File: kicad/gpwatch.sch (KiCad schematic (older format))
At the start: 4 parts

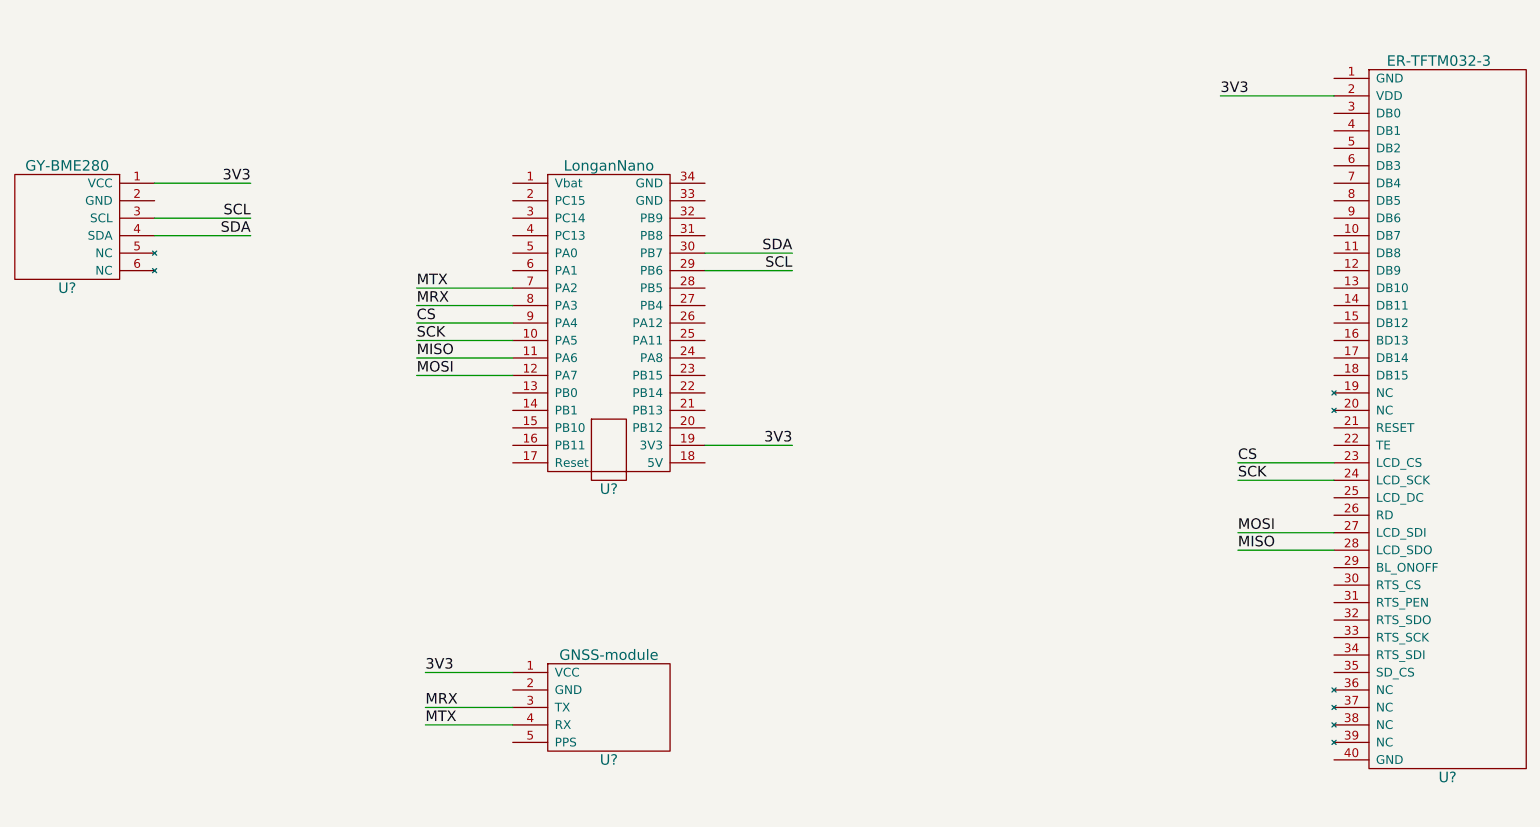
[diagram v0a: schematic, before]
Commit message: add backup battery jack, 3 buttons
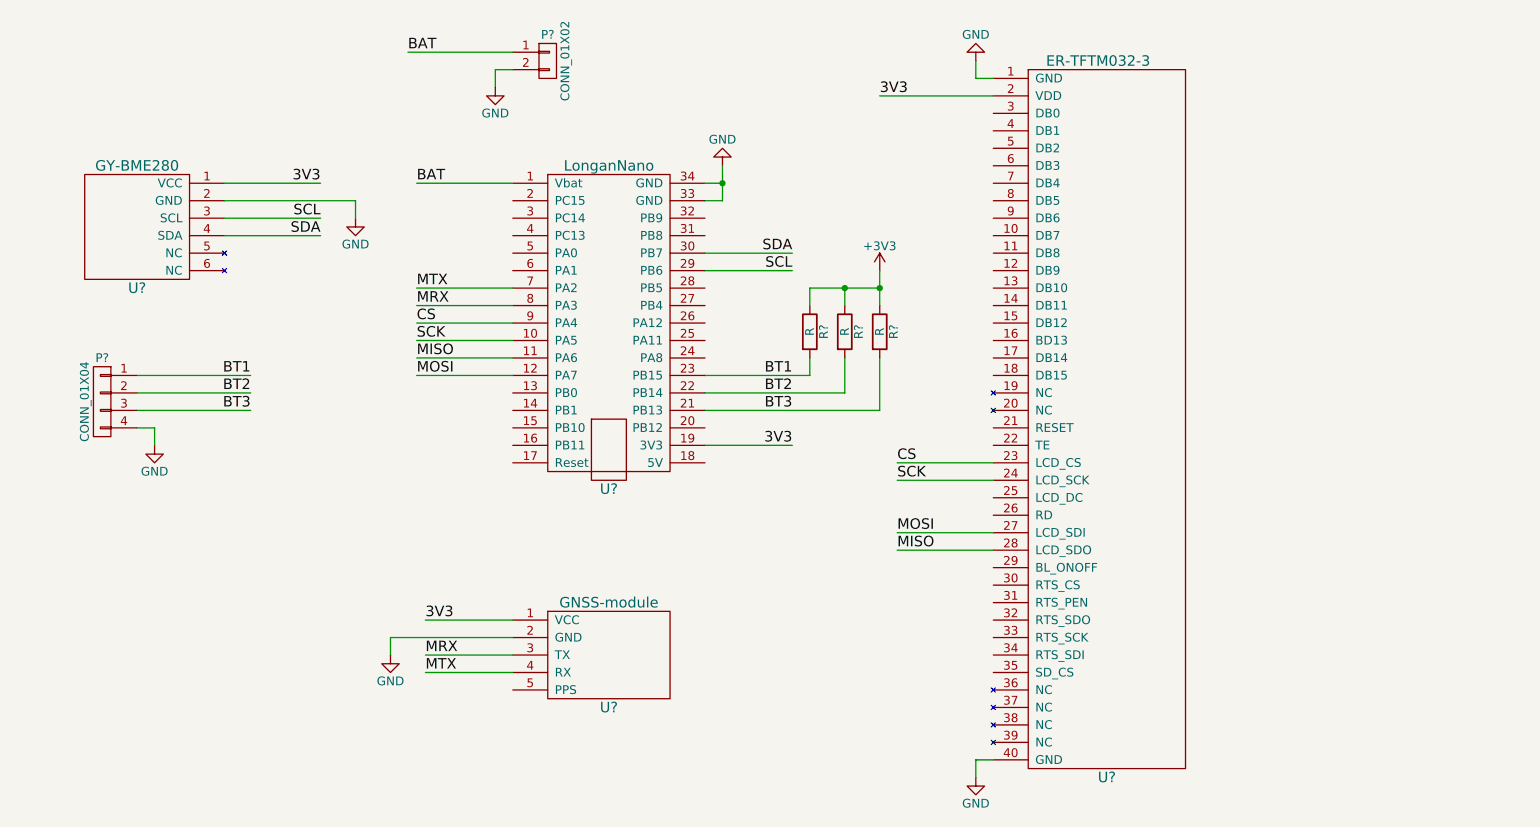
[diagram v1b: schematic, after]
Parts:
- added P?: CONN_01X02, symbol CONN_01X02
- added P?: CONN_01X04, symbol CONN_01X04
- added R? (x3): R, symbol R
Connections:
- net BAT: now reaches U?.1 (Vbat)
- net BAT: now also P?.1 (P1)
- net BT3: now reaches U?.21 (PB13)
- net BT3: now also P?.3 (P3), R?.2
- net BT2: now reaches U?.22 (PB14)
- net BT2: now also P?.2 (P2), R?.2
- net BT1: now reaches U?.23 (PB15)
- net BT1: now also P?.1 (P1), R?.2
- net GND: now reaches U?.33 (GND)
- net GND: now also U?.1 (GND), U?.2 (GND), U?.2 (GND), U?.34 (GND), U?.40 (GND), P?.2 (P2), P?.4 (P4)
- new net +3V3: R?.1, R?.1, R?.1
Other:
- moved on the sheet: U?

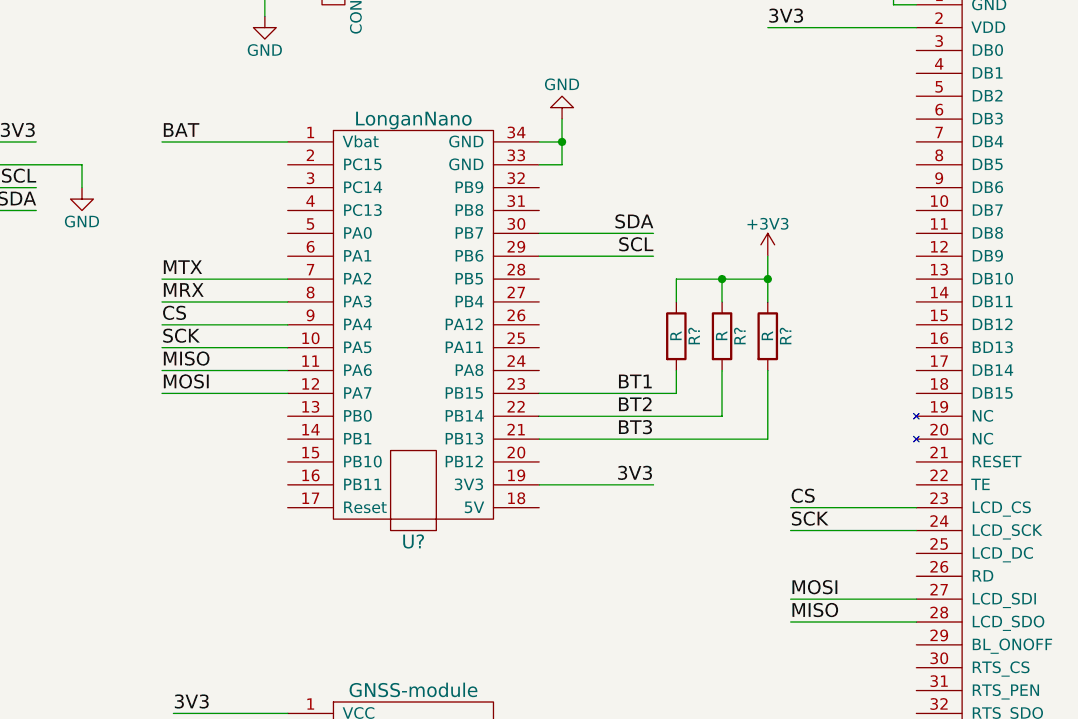
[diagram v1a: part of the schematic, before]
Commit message: add bsp source code
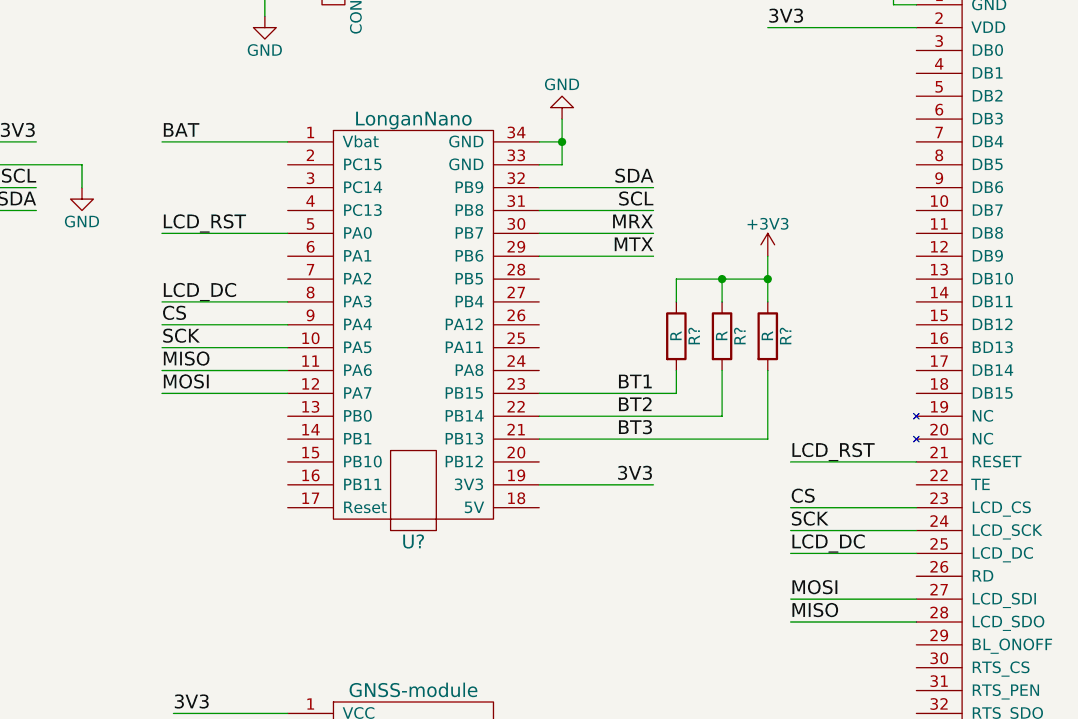
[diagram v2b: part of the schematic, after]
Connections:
- net MRX: now also U?.30 (PB7); no longer U?.8 (PA3)
- net MTX: now also U?.29 (PB6); no longer U?.7 (PA2)
- net SCL: now also U?.31 (PB8); no longer U?.29 (PB6)
- net SDA: now also U?.32 (PB9); no longer U?.30 (PB7)
- net LCD_RST: now reaches U?.5 (PA0)
- net LCD_RST: now also U?.21 (RESET)
- net LCD_DC: now reaches U?.25 (LCD_DC)
- net LCD_DC: now also U?.8 (PA3)
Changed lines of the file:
@@
 Text Label 7000 3650 0    60   ~ 0
 CS
-Text Label 4250 2650 0    60   ~ 0
+Text Label 6400 2550 2    60   ~ 0
 MTX
-Text Label 4250 2750 0    60   ~ 0
+Text Label 6400 2450 2    60   ~ 0
 MRX
 Text Label 4300 4750 0    60   ~ 0
@@
 Text Label 4300 4850 0    60   ~ 0
 MTX
-Text Label 6400 2450 2    60   ~ 0
+Text Label 6400 2250 2    60   ~ 0
 SDA
-Text Label 6400 2550 2    60   ~ 0
+Text Label 6400 2350 2    60   ~ 0
 SCL
 Text Label 3700 2250 2    60   ~ 0
@@
 	4250 2850 4800 2850
 Wire Wire Line
-	4250 2650 4800 2650
-Wire Wire Line
-	4250 2750 4800 2750
-Wire Wire Line
 	4300 4750 4800 4750
 Wire Wire Line
 	4300 4850 4800 4850
 Wire Wire Line
-	6400 2450 5900 2450
-Wire Wire Line
-	6400 2550 5900 2550
+	6400 2250 5900 2250
 Wire Wire Line
 	3700 2250 3150 2250
@@
 Text Label 6400 3350 2    60   ~ 0
 BT3
+Wire Wire Line
+	6400 2350 5900 2350
+Wire Wire Line
+	6400 2450 5900 2450
+Wire Wire Line
+	6400 2550 5900 2550
+Wire Wire Line
+	7000 3850 7550 3850
+Text Label 7000 3850 0    60   ~ 0
+LCD_DC
+Wire Wire Line
+	4250 2750 4800 2750
+Text Label 4250 2750 0    60   ~ 0
+LCD_DC
+Wire Wire Line
+	7000 3450 7550 3450
+Text Label 7000 3450 0    60   ~ 0
+LCD_RST
+Wire Wire Line
+	4250 2450 4800 2450
+Text Label 4250 2450 0    60   ~ 0
+LCD_RST
 $EndSCHEMATC

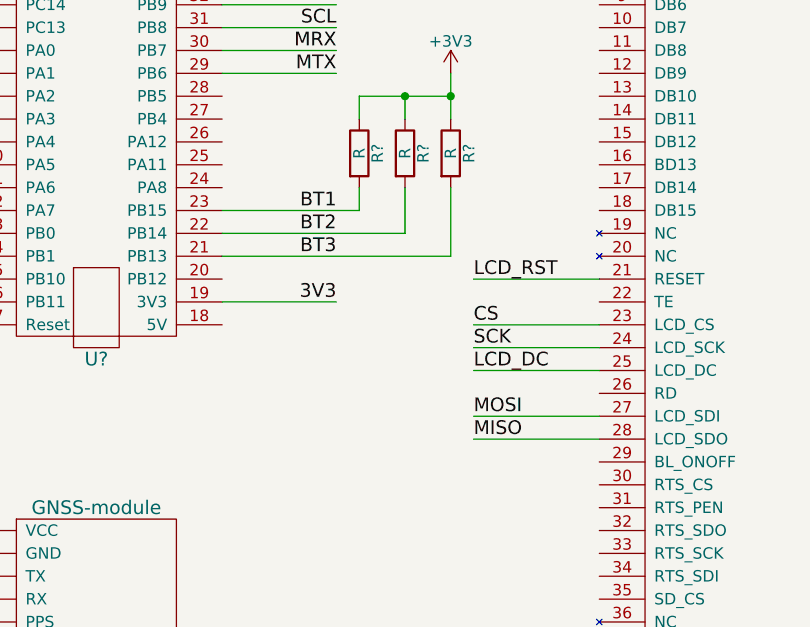
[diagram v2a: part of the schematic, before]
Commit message: add display support code, not all
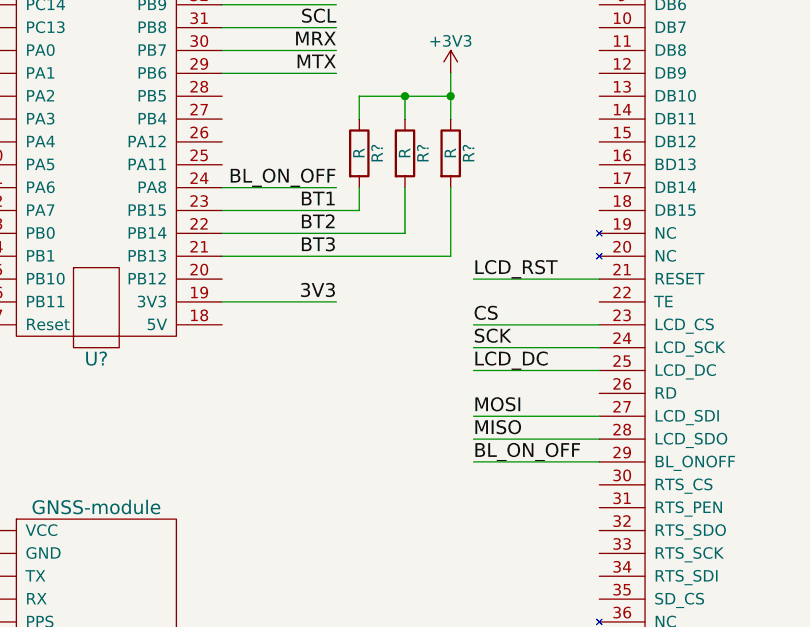
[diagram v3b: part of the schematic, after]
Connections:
- net BL_ON_OFF: now reaches U?.24 (PA8)
- net BL_ON_OFF: now also U?.29 (BL_ONOFF)
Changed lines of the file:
@@
 Text Label 4250 2450 0    60   ~ 0
 LCD_RST
+Wire Wire Line
+	7000 4250 7550 4250
+Text Label 7000 4250 0    60   ~ 0
+BL_ON_OFF
+Text Label 6400 3050 2    60   ~ 0
+BL_ON_OFF
+Wire Wire Line
+	6400 3050 5900 3050
 $EndSCHEMATC
